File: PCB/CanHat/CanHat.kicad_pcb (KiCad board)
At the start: 2 copper layers, 65 x 56.5 mm, 26 parts, among them J1 Raspberry_Pi_2_3, J10 Conn_01x02, J2 Conn_01x02, J3 Conn_01x02, J4 Conn_01x02, J5 Conn_01x02, J6 Conn_01x02, J7 Conn_01x02, J8 Conn_01x02, J9 Conn_01x02, U1 MCP2515-xSO, U2 SN65HVD230, Y1 Crystal

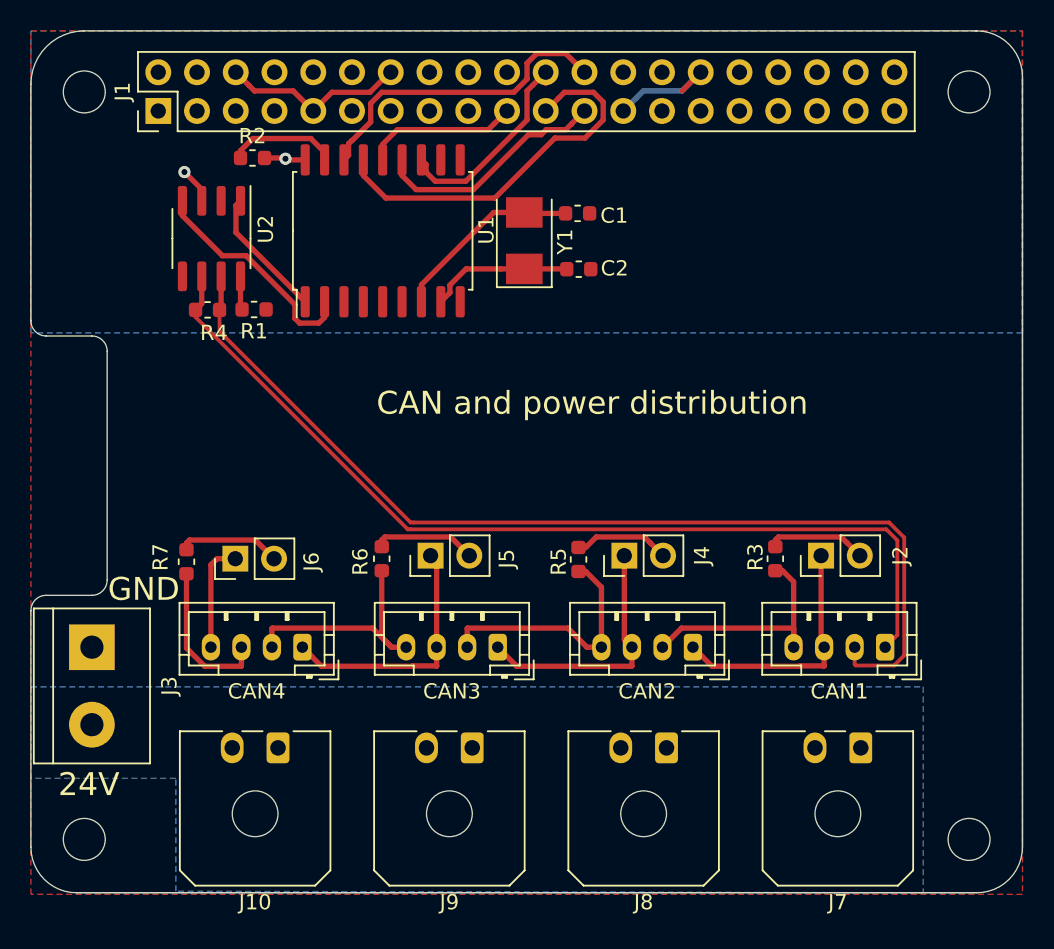
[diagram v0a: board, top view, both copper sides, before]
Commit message: Working on 0.4 Thermistor contact moved along the power contacts(can/heater) Added a micro USB connector, useful for flashing Added an on board 3.3V regulator
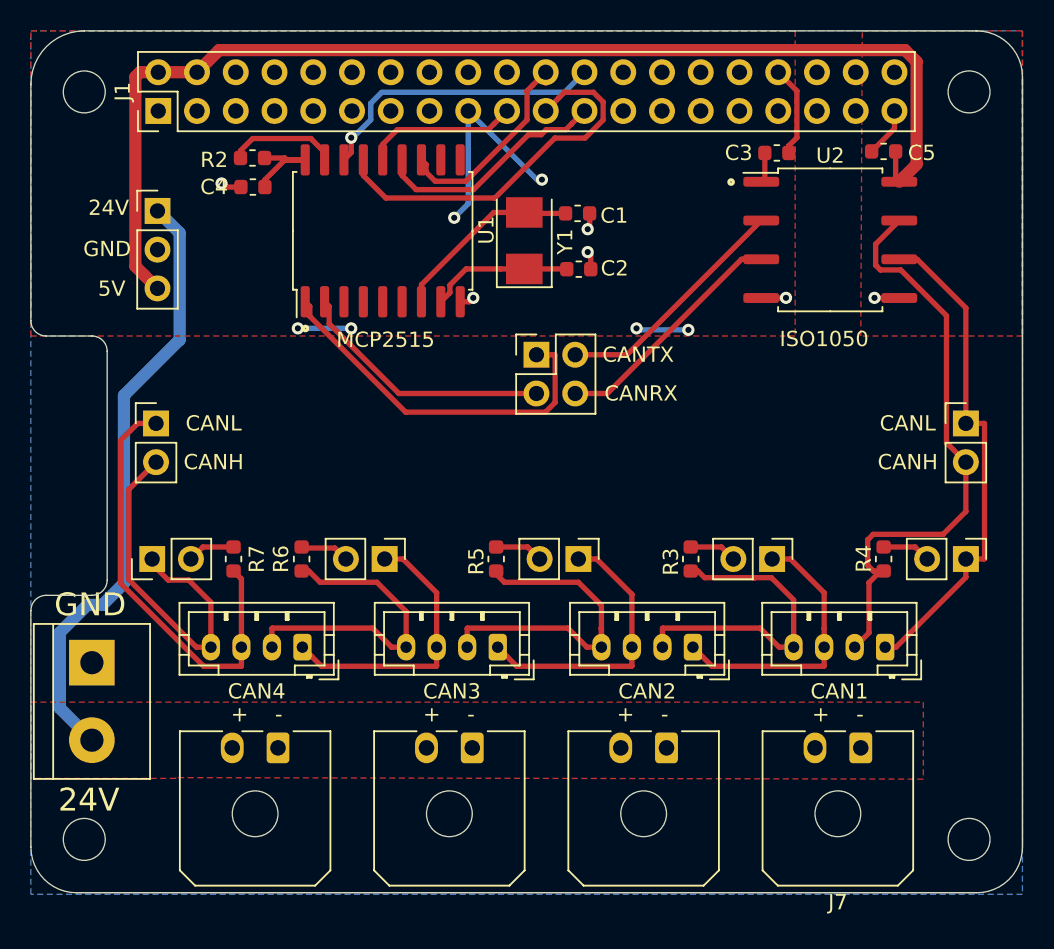
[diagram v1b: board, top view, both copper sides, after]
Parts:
- removed R1: 1k, Resistor_SMD:R_0603_1608Metric
- added C3: 0.1uF, Capacitor_SMD:C_0603_1608Metric, F.Cu at (148.9, 108.0)
- added C4: 0.1uF, Capacitor_SMD:C_0603_1608Metric, F.Cu at (114.6, 110.2)
- added C5: 0.1uF, Capacitor_SMD:C_0603_1608Metric, F.Cu at (155.9, 107.9)
- added J11: Conn_02x02_Odd_Even, Connector_PinHeader_2.54mm:PinHeader_2x02_P2.54mm_Vertical, F.Cu at (133.1, 121.2)
- added J12: Conn_01x02, Connector_PinHeader_2.54mm:PinHeader_1x02_P2.54mm_Vertical, F.Cu at (161.3, 134.6)
- added J13: Conn_01x02, Connector_PinHeader_2.54mm:PinHeader_1x02_P2.54mm_Vertical, F.Cu at (161.3, 125.7)
- added J14: Conn_01x02, Connector_PinHeader_2.54mm:PinHeader_1x02_P2.54mm_Vertical, F.Cu at (108.2, 125.7)
- added J15: Conn_01x04, Connector_PinHeader_2.54mm:PinHeader_1x03_P2.54mm_Vertical, F.Cu at (108.3, 111.8)
- C1, C2: value C -> 22p
- U2: value SN65HVD230 -> ISO1050DUB; footprint Package_SO:SOIC-8_3.9x4.9mm_P1.27mm -> Package_SO:SOP-8_6.62x9.15mm_P2.54mm
- moved R4 47.2 mm to (155.9, 134.6), turned to 90 degrees
- moved U2 40.6 mm to (152.4, 113.7), turned to 0 degrees
- moved R3 5.54 mm to (143.3, 134.6)
- moved J6 5.45 mm to (108.0, 134.6)
- moved R5 5.40 mm to (130.5, 134.6)
- moved R6 5.25 mm to (117.8, 134.6)
- moved J2 3.22 mm to (148.6, 134.6), turned to 270 degrees
- moved R7 3.09 mm to (113.3, 134.6)
- moved J4 3.02 mm to (135.9, 134.6), turned to 270 degrees
- moved J5 3.02 mm to (123.2, 134.6), turned to 270 degrees
- moved J3 1.02 mm to (104.0, 141.4)
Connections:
- net Net-(J10-Pad2) renamed VDC
- J1 pad 2: (no net) -> +5V
- J1 pad 4: (no net) -> +5V
- R4 pad 2: CANL -> Net-(J12-Pad2)
- U1 pad 1: Net-(U1-Pad1) -> Net-(J11-Pad1)
- U1 pad 2: Net-(U1-Pad2) -> Net-(J11-Pad3)
- U2 pad 1: Net-(U1-Pad1) -> +3V3
- U2 pad 2: GND -> /CANTX
- U2 pad 3: +3V3 -> /CANRX
- U2 pad 4: Net-(U1-Pad2) -> GND
- U2 pad 5: (no net) -> GND
- U2 pad 8: Net-(R1-Pad2) -> +5V
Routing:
- net +5V: track 0.00 -> 77.2 mm
- net VDC: track 0.00 -> 40.0 mm
- net CANL: track 62.2 -> 33.0 mm
- net CANH: track 66.5 -> 38.9 mm
- net Net-(J11-Pad1): track 0.00 -> 24.4 mm
- net +3V3: track 5.08 -> 29.4 mm, vias 2 -> 6
- net Net-(CAN4-Pad3): track 10.2 -> 28.8 mm
- net Net-(J11-Pad3): track 0.00 -> 17.0 mm
- net Net-(CAN4-Pad4): track 7.17 -> 23.8 mm
- net /CANTX: track 0.00 -> 15.8 mm
- net /CANRX: track 0.00 -> 15.8 mm
- net Net-(U1-Pad2): track 14.9 -> 0.00 mm
- net Net-(U1-Pad1): track 8.62 -> 0.00 mm
- net Net-(CAN2-Pad4): track 16.4 -> 22.6 mm
- net Net-(CAN3-Pad4): track 15.9 -> 20.8 mm
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- added copper zone on F.Cu, net +3V3
- added copper zone on F.Cu, net +5V
- added copper zone on B.Cu, net GND
- added copper zone on F.Cu, net VDC
- removed copper zone on B.Cu, net +3V3
- removed copper zone on F.Cu, net GND
- removed copper zone on B.Cu, net VDC
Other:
- board text added: "+ -"
- board text added: "5V"
- board text added: "CANH"
- board text added: "CANL"
- board text added: "CANRX"
- board text added: "CANTX"
- board text added: "ISO1050"
- board text added: "MCP2515"
- board text removed: "CAN and power distribution"

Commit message: schematics pdf
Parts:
- added F1: Fuse, Fuse:Fuseholder_Blade_Mini_Keystone_3568, F.Cu at (110.0, 151.0)
- J10, J7, J8, J9: footprint Connector_Molex:Molex_Micro-Fit_3.0_43650-0200_1x02_P3.00mm_Horizontal -> Connector_Molex:Molex_Micro-Fit_3.0_43650-0215_1x02_P3.00mm_Vertical
- moved J6 8.05 mm to (116.0, 134.6), turned to 270 degrees
- moved CAN4 6.00 mm to (123.8, 140.4)
- moved R6 4.75 mm to (122.5, 134.6)
- moved J5 4.64 mm to (127.8, 134.6)
- moved J10 4.53 mm to (119.2, 150.4), turned to 0 degrees
- moved J7 4.25 mm to (151.8, 150.4), turned to 0 degrees
- moved CAN3 4.10 mm to (134.7, 140.4)
- moved R5 3.80 mm to (134.3, 134.6)
- moved J4 3.67 mm to (139.6, 134.6)
- moved J9 3.58 mm to (130.1, 150.4), turned to 0 degrees
- moved J8 3.47 mm to (140.9, 150.4), turned to 0 degrees
- moved R7 2.68 mm to (110.6, 134.6)
- moved CAN2 2.20 mm to (145.6, 140.4)
- moved J2 1.70 mm to (150.3, 134.5)
- moved R3 1.70 mm to (145.0, 134.5)
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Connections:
- J3 pad 2: VDC -> Net-(F1-Pad1)
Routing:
- net Net-(F1-Pad1): track 0.00 -> 11.3 mm
- net Net-(J11-Pad1): track 24.4 -> 17.2 mm
- net Net-(J11-Pad3): track 17.0 -> 21.7 mm
- net Net-(CAN2-Pad4): track 22.6 -> 18.2 mm
- net Net-(CAN4-Pad4): track 23.8 -> 19.9 mm
- net Net-(CAN1-Pad3): track 18.8 -> 15.6 mm
- net VDC: track 40.0 -> 36.9 mm
- net Net-(CAN2-Pad3): track 18.5 -> 15.5 mm
- net Net-(CAN3-Pad3): track 18.4 -> 15.8 mm
- net Net-(CAN1-Pad4): track 21.0 -> 18.5 mm
- net Net-(CAN3-Pad4): track 20.8 -> 18.7 mm
- net Net-(CAN4-Pad3): track 28.8 -> 27.7 mm
- net /CANTX: track 15.8 -> 15.3 mm
- net /CANRX: track 15.8 -> 15.3 mm
- added copper zone on F.Cu, net Net-(F1-Pad1)
- removed copper zone on F.Cu, net +5V
